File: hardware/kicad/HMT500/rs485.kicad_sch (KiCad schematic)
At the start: 6 parts, among them U11 THVD2450DR

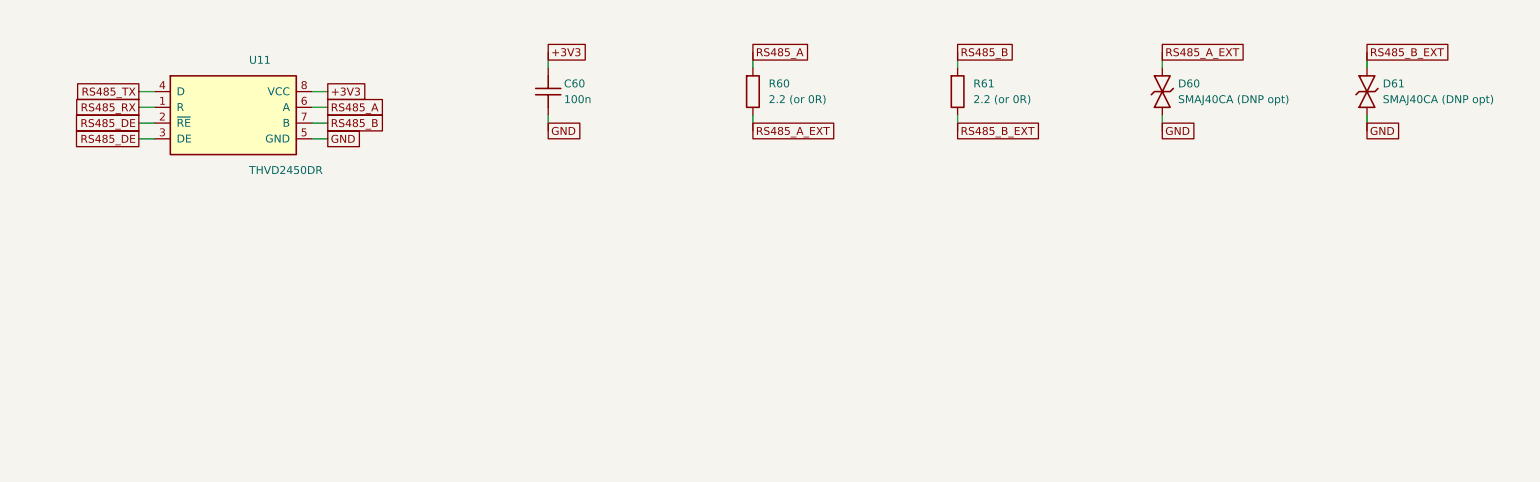
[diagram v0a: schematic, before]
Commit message: KiCad schematic v0.2: hand-laid-out, wired, readable sheets with power symbols and functional blocks
Replaces the label-only v0.1. Drawing rules are validated at generation and
the drawn netlist is checked against design intent (71 nets, 0 errors).

Co-Authored-By: Claude Opus 5.5 <noreply@anthropic.com>
Claude-Session: https://claude.ai/code/session_01JA2o8uJsqp9Vzsg4b665ev
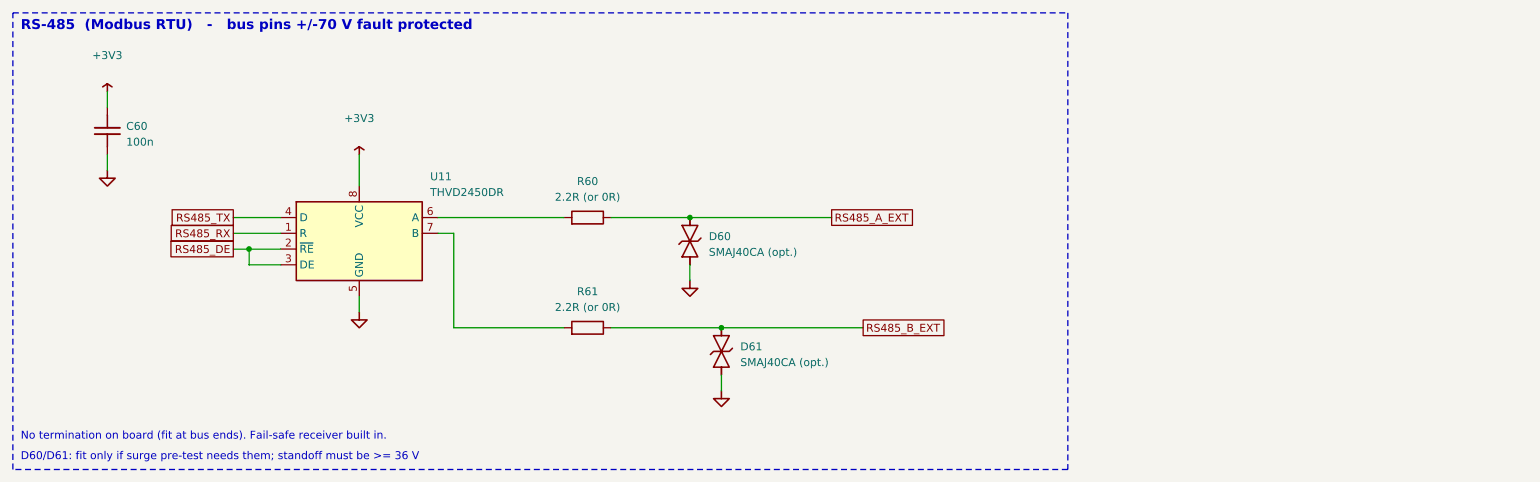
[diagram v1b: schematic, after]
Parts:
- D60, D61: value SMAJ40CA (DNP opt) -> SMAJ40CA (opt.); Note DNP if surge pre-test passes without it -> (none)
- R60, R61: value 2.2 (or 0R) -> 2.2R (or 0R)
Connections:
- net RS485_A: no longer names the net of R60.1, U11.6 (A)
- net RS485_B: no longer names the net of R61.1, U11.7 (B)
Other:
- note added: "D60/D61: fit only if surge pre-test needs them; standoff must be >= 36 V"
- note added: "No termination on board (fit at bus ends). Fail-safe receiver built in."
- note added: "RS-485 (Modbus RTU) - bus pins +/-70 V fault protected"
- title: HMT500 - RS-485 (+/-70V fault protected) -> HMT500  RS-485
- moved on the sheet: C60, R60, R61, U11

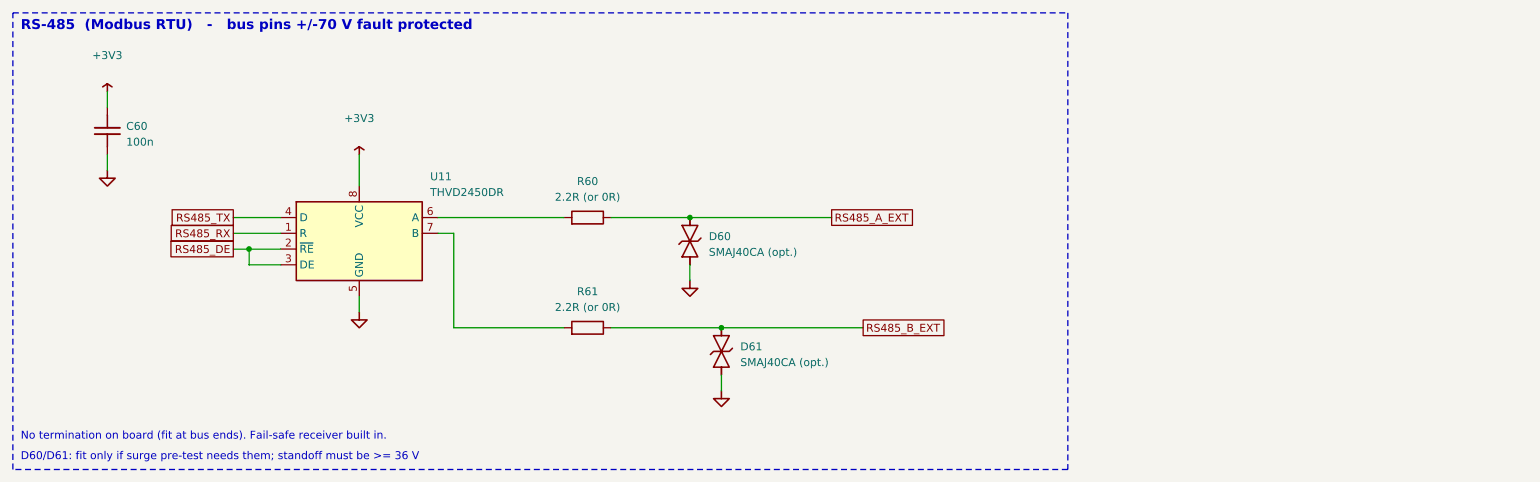
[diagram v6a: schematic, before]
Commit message: Schematic drawing rules: no overlapping text, Korean font, distinct net names
- Generator places reference/value text automatically, clear of symbol bodies,
  pins, wires, labels, notes and box edges; validation fails on any overlap
  (also note text vs wires/power names and bodies vs box edges)
- Fix 180-degree parts (LED) whose justification KiCad mirrors
- Styles: reference bold, value normal, power nets italic, signal nets boxed labels
- Korean box subtitles and legend in NanumGothic TrueType (stroke font has no Hangul)
- Nets renamed where they matched part or pin names: LED -> STAT_LED, EF_ILIM/IMON/DVDT
- J1 GH mounting pads removed from the symbol (PCB only); connector sheet re-spaced
- Schematic PDF export added; tests for net naming and Hangul font

Co-Authored-By: Claude Opus 5.5 <noreply@anthropic.com>
Claude-Session: https://claude.ai/code/session_01JA2o8uJsqp9Vzsg4b665ev
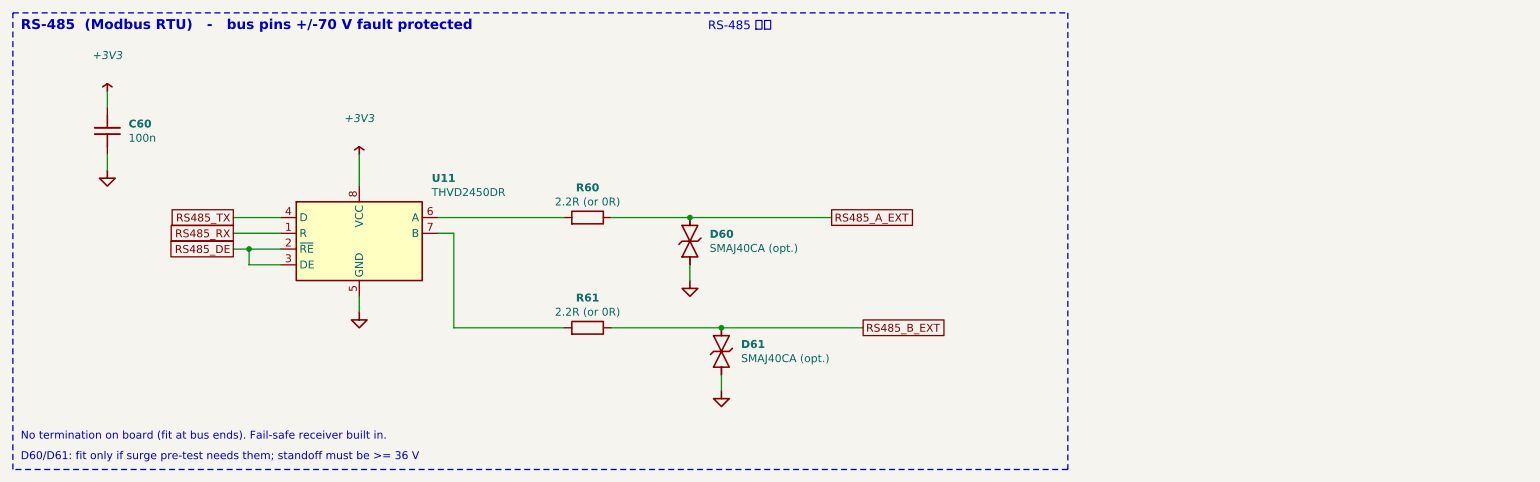
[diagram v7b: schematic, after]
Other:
- note added: "RS-485 통신"

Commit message: Schematic v0.6: parts cleanup (91 -> 75) and PCB temperature sensing
- Removed: fault pull-ups R11-R15 (MCU internal pull-ups), status LED D3/R16
  (not visible after potting), RS-485 R60/R61/D60/D61 (THVD2450 built-in
  protection), VREF+ filter FB2/C19 (MCU ADC only for diagnostics), C11/C2/C6
  (duplicated by adjacent capacitors); VREF+ tied to +3V3 with C20
- PCB temperature with no added parts: ADS1220 internal sensor at the measurement
  front, STM32G0 internal sensor mid-board; compensation plan in circuit-design 5B
- 63 nets, netlist check 0 errors; parts list regenerated; decision log #22/#23

Co-Authored-By: Claude Opus 5.5 <noreply@anthropic.com>
Claude-Session: https://claude.ai/code/session_01JA2o8uJsqp9Vzsg4b665ev
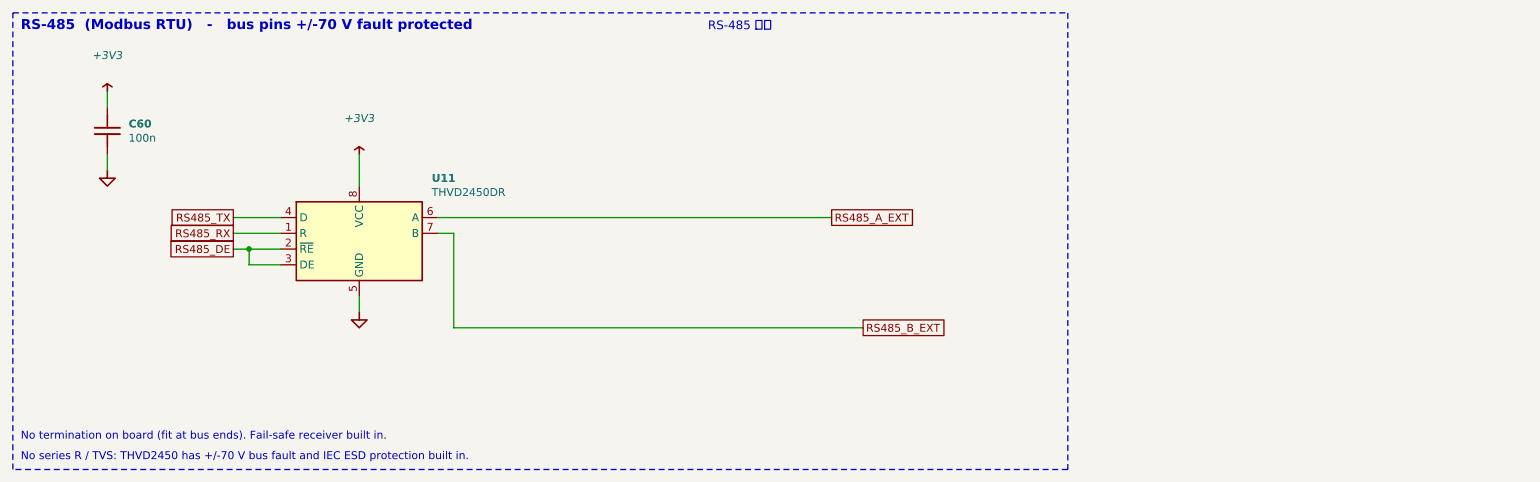
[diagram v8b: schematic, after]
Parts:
- removed D60, D61: SMAJ40CA (opt.), Diode_SMD:D_SMA, symbol HMT500:TVS_BI
- removed R60, R61: 2.2R (or 0R), Resistor_SMD:R_0603_1608Metric, symbol HMT500:R
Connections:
- net RS485_A_EXT: now also U11.6 (A)
- net RS485_B_EXT: now also U11.7 (B)
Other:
- note added: "No series R / TVS: THVD2450 has +/-70 V bus fault and IEC ESD protection built in."
- note removed: "D60/D61: fit only if surge pre-test needs them; standoff must be >= 36 V"
